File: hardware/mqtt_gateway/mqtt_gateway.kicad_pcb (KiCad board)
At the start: 2 copper layers, 75 x 51 mm, 54 parts, among them J1 awesome:RJ45-CAN, J3 RJ45_Amphenol_RJMG1BD3B8K1ANR, J4 WAGO250-204, Q1 BC847, Q2 BC847, U1 wuerthDebug6, U2 LD1117S33TR_SOT223, U3 PESD2CAN, U4 MCP2562-E-SN, U6 ESP32-WROOM-32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

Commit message: feat: Switch to 4 layer stackup
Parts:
- removed FB2: Ferrite_Bead_Small, Capacitor_SMD:C_0805_2012Metric_Pad1.18x1.45mm_HandSolder
- removed L1: 1m, Inductor_SMD:L_1210_3225Metric_Pad1.42x2.65mm_HandSolder
- added C7: 100n, Capacitor_SMD:C_0402_1005Metric_Pad0.74x0.62mm_HandSolder, F.Cu at (115.3, 109.5)
- added C8: 100n, Capacitor_SMD:C_0402_1005Metric_Pad0.74x0.62mm_HandSolder, F.Cu at (112.3, 103.8)
- added J2: Button-Sensors-MicroMatch2X03, awesome:02x03MicroMatch, F.Cu at (103.1, 89.7)
- added J5: Button-Sensors-MicroMatch2X03, awesome:02x03MicroMatch, F.Cu at (167.4, 86.5)
- added R1: 100R, Resistor_SMD:R_0603_1608Metric_Pad0.98x0.95mm_HandSolder, F.Cu at (111.0, 84.6)
- added R24: 100R, Resistor_SMD:R_0603_1608Metric_Pad0.98x0.95mm_HandSolder, F.Cu at (175.4, 81.5)
- added R25: 10K, Resistor_SMD:R_0603_1608Metric_Pad0.98x0.95mm_HandSolder, F.Cu at (126.9, 113.6)
- added R28: 10K, Resistor_SMD:R_0603_1608Metric_Pad0.98x0.95mm_HandSolder, F.Cu at (117.6, 110.6)
- added R29: 100R, Resistor_SMD:R_0603_1608Metric_Pad0.98x0.95mm_HandSolder, F.Cu at (176.2, 93.6)
- added R30: 100R, Resistor_SMD:R_0603_1608Metric_Pad0.98x0.95mm_HandSolder, F.Cu at (172.7, 81.5)
- added R31: 100R, Resistor_SMD:R_0603_1608Metric_Pad0.98x0.95mm_HandSolder, F.Cu at (173.9, 93.3)
- added R4: 100R, Resistor_SMD:R_0603_1608Metric_Pad0.98x0.95mm_HandSolder, F.Cu at (108.5, 84.6)
- added R5: 100R, Resistor_SMD:R_0603_1608Metric_Pad0.98x0.95mm_HandSolder, F.Cu at (107.1, 96.4)
- C12: value 1n -> 10u
- C14, C15, C17: footprint Capacitor_SMD:C_0603_1608Metric_Pad1.08x0.95mm_HandSolder -> Capacitor_SMD:C_0402_1005Metric_Pad0.74x0.62mm_HandSolder
- C16: value 1n -> 1u; footprint Capacitor_SMD:C_0603_1608Metric_Pad1.08x0.95mm_HandSolder -> Capacitor_SMD:C_0402_1005Metric_Pad0.74x0.62mm_HandSolder
- R16, R2: footprint Resistor_SMD:R_0603_1608Metric_Pad0.98x0.95mm_HandSolder -> Resistor_SMD:R_0402_1005Metric_Pad0.72x0.64mm_HandSolder
- R18: footprint Resistor_SMD:R_0603_1608Metric_Pad0.98x0.95mm_HandSolder -> Resistor_SMD:R_0402_1005Metric_Pad0.72x0.64mm_HandSolder; moved to F.Cu
- R3: value 33R -> 100R
- moved R9 39.0 mm to (134.8, 74.5), turned to -90 degrees
- moved R16 38.3 mm to (113.3, 109.5), turned to 90 degrees
- moved R6 24.6 mm to (126.1, 102.9), turned to 180 degrees
- moved R3 23.3 mm to (109.6, 96.4), turned to -90 degrees
- moved R8 21.7 mm to (113.4, 81.3), turned to 90 degrees
- moved R19 16.9 mm to (126.1, 101.4), turned to 180 degrees
- moved FB1 12.8 mm to (117.6, 98.8), turned to 90 degrees
- moved R2 11.4 mm to (114.3, 109.5), turned to 90 degrees
- moved C17 6.33 mm to (117.6, 102.7), turned to 0 degrees
- moved C16 5.98 mm to (117.6, 101.7)
- moved R18 5.78 mm to (116.3, 110.0), turned to -90 degrees
- moved C9 4.92 mm to (158.0, 89.4), turned to 180 degrees
- moved C18 4.83 mm to (122.6, 94.2), turned to 180 degrees
- moved C15 3.35 mm to (111.6, 108.1)
- moved C1 3.25 mm to (166.3, 90.0)
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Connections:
- net Net-(R16-Pad1) renamed /RXD1
- net Net-(R19-Pad2) renamed /ETHCLK_50M
- net Net-(U6-Pad33) renamed /TXEN
- C16 pad 1: Net-(C16-Pad1) -> VDDA
- C17 pad 1: Net-(C16-Pad1) -> VDDA
- FB1 pad 1: +3.3V -> VDDA
- FB1 pad 2: Net-(FB1-Pad2) -> +3.3V
- R18 pad 1: Net-(R18-Pad1) -> /RXER
- R18 pad 2: VDDA -> +3.3V
- R2 pad 1: Net-(R2-Pad1) -> /RXD0
- R3 pad 1: Net-(R3-Pad1) -> Net-(J2-Pad4)
- R3 pad 2: Net-(R3-Pad2) -> /B2-0/SCL
- R6 pad 1: Net-(R6-Pad1) -> /NRST
- U6 pad 10: Net-(U6-Pad10) -> /RXD0
- U6 pad 12: Net-(R18-Pad1) -> /CRS
- U6 pad 23: unconnected-(U6-Pad23) -> /B3-0
- U6 pad 24: unconnected-(U6-Pad24) -> /B2-0/SCL
- U6 pad 26: /SCK -> /B1-0/SDA
- U6 pad 27: unconnected-(U6-Pad27) -> /B4-0
- U6 pad 29: /SS -> /NRST
- U6 pad 30: Net-(U6-Pad30) -> /MDIO
- U6 pad 31: Net-(U6-Pad31) -> /TXD0
- U6 pad 36: Net-(R2-Pad1) -> /TXD1
- U6 pad 37: Net-(R3-Pad1) -> /MDC
- U6 pad 6: unconnected-(U6-Pad6) -> /B4-1
- U6 pad 7: unconnected-(U6-Pad7) -> /B3-1
- U6 pad 8: Net-(U6-Pad8) -> /B2-1/SCL
- U6 pad 9: Net-(R6-Pad1) -> /B1-1/SDA
- U7 pad 10: Net-(U6-Pad10) -> /RXER
- U7 pad 11: Net-(R16-Pad2) -> /CRS
- U7 pad 12: Net-(R18-Pad1) -> /MDIO
- U7 pad 13: Net-(U6-Pad8) -> /MDC
- U7 pad 15: Net-(R6-Pad1) -> /NRST
- U7 pad 17: Net-(U6-Pad30) -> /TXD0
- U7 pad 18: Net-(U6-Pad31) -> /TXD1
- U7 pad 7: Net-(R3-Pad2) -> Net-(R16-Pad2)
- U7 pad 9: Net-(FB1-Pad2) -> VDDA
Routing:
- net /B2-1/SCL: track 0.00 -> 52.9 mm, vias 0 -> 2
- net GND: track 51.5 -> 99.8 mm, vias 6 -> 22
- net /B3-1: track 0.00 -> 46.7 mm, vias 0 -> 2
- net /B1-1/SDA: track 0.00 -> 44.9 mm, vias 0 -> 2
- net /B3-0: track 0.00 -> 42.4 mm, vias 0 -> 2
- net Net-(R16-Pad2): track 43.9 -> 1.72 mm, vias 2 -> 0
- net /B1-0/SDA: track 0.00 -> 41.7 mm, vias 0 -> 2
- net +3.3V: track 170.2 -> 210.8 mm, vias 5 -> 9
- net Net-(R6-Pad1): track 39.6 -> 0.00 mm, vias 2 -> 0
- net /RXD0: track 0.00 -> 38.1 mm, vias 0 -> 2
- net /RXD1: track 3.52 -> 41.3 mm, vias 0 -> 2
- net Net-(U6-Pad10): track 37.2 -> 0.00 mm, vias 2 -> 0
- net Net-(R18-Pad1): track 36.4 -> 0.00 mm, vias 2 -> 0
- net /CRS: track 0.00 -> 35.5 mm, vias 0 -> 2
- net Net-(U6-Pad8): track 34.3 -> 0.00 mm, vias 2 -> 0
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- added copper zone on In1.Cu, net GND
- added copper zone on In2.Cu, net GND
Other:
- copper layers 2 -> 4

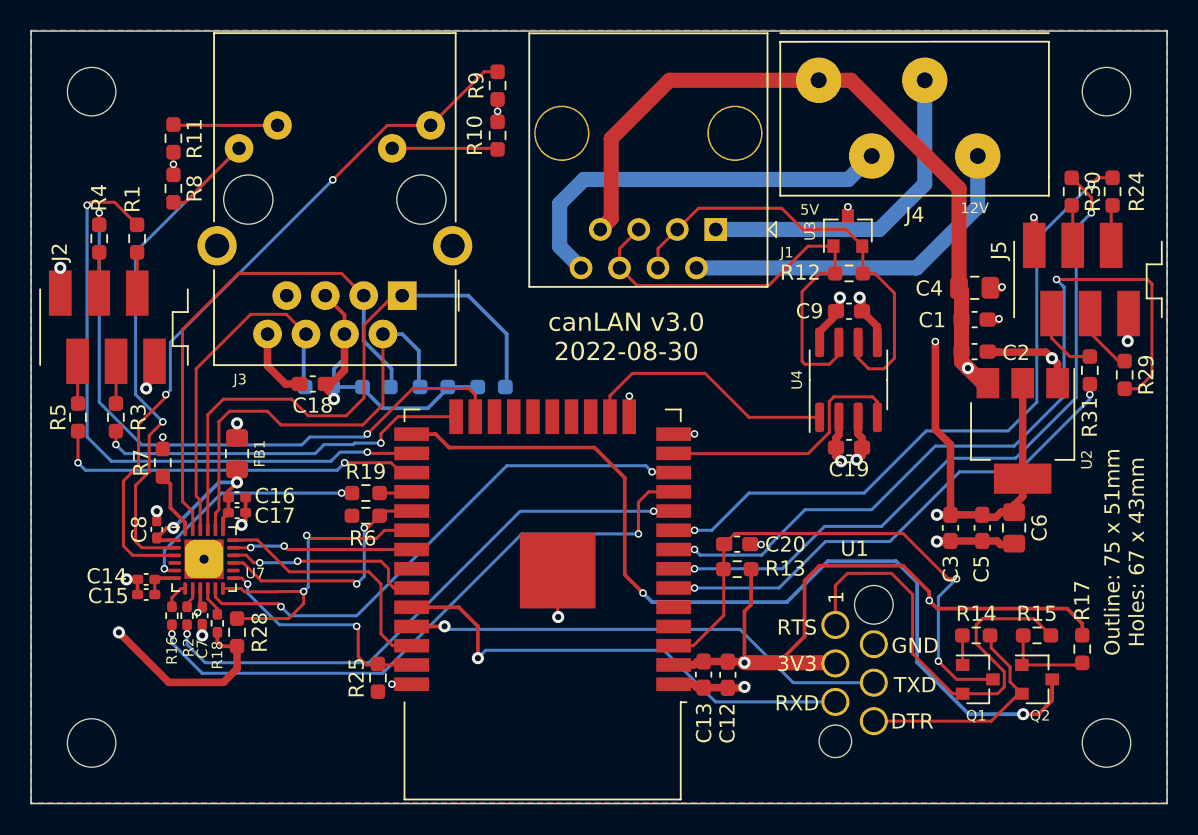
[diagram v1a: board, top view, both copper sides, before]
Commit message: style: Move traces
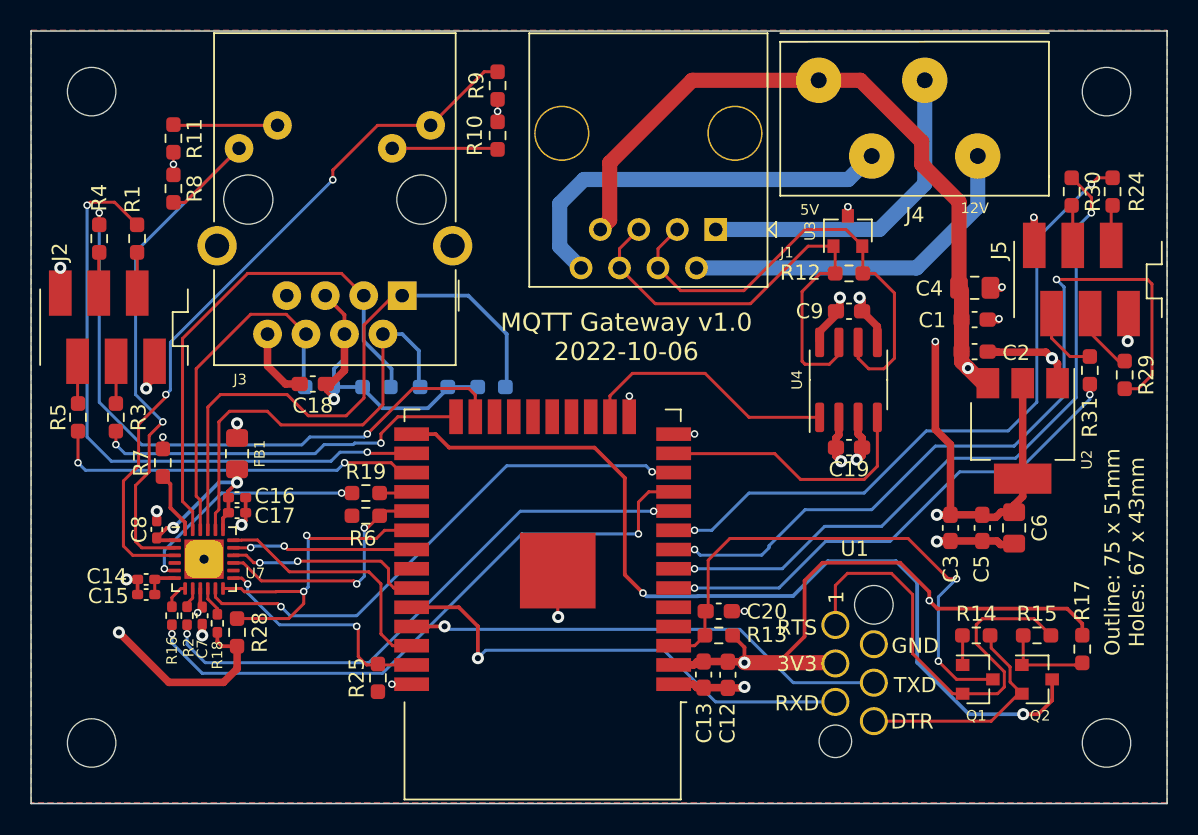
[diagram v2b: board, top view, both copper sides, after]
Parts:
- moved C20 4.59 mm to (149.4, 109.2)
- moved R13 4.54 mm to (149.4, 110.8)
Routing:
- net +3.3V: track 210.8 -> 206.7 mm
- net Net-(J1-Pad3): track 29.7 -> 32.1 mm
- net Net-(J1-Pad5): track 31.5 -> 32.5 mm
- net Net-(J3-PadR1): track 38.9 -> 39.4 mm
- net +5V: track 61.9 -> 61.3 mm
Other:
- board text added: "MQTT Gateway v1.0 2022-10-06"
- board text removed: "canLAN v3.0 2022-08-30"

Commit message: feat: change PCB debug to EN/BOOT0
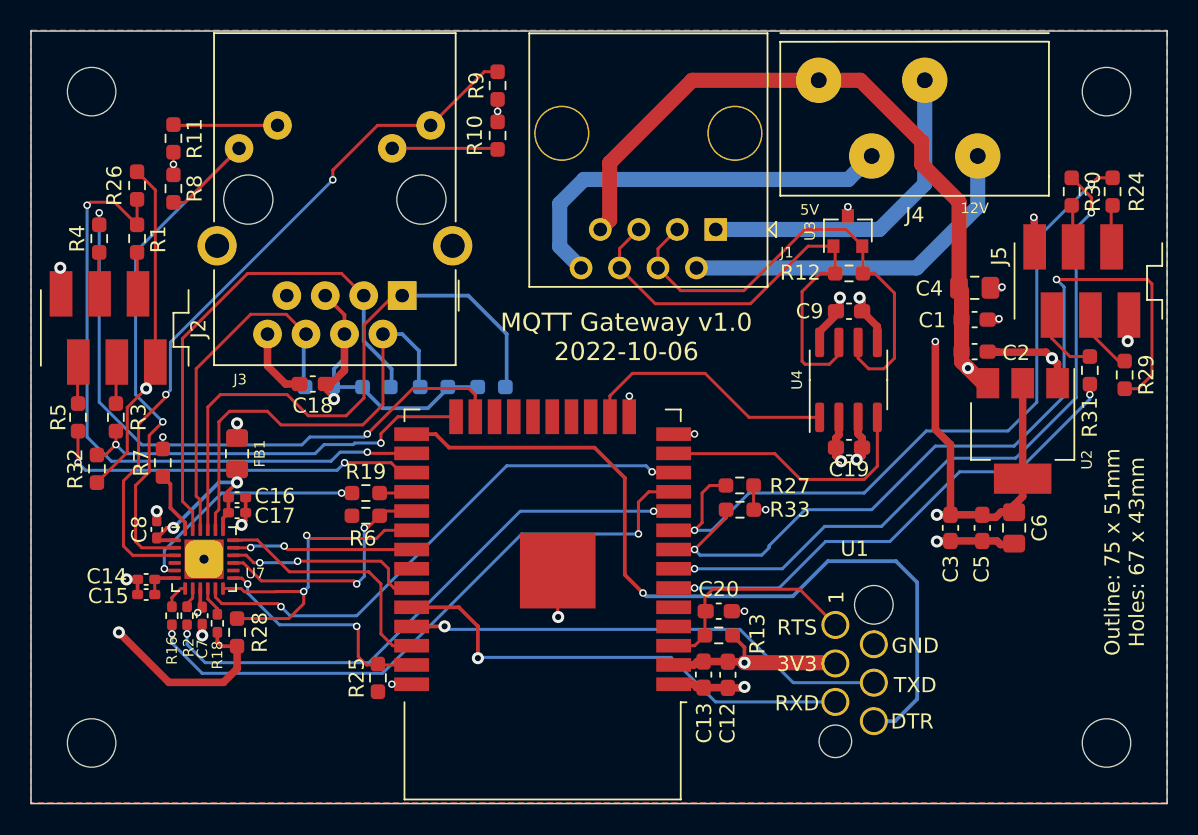
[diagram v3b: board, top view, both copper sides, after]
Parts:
- removed Q1, Q2: BC847, Package_TO_SOT_SMD:SOT-23
- removed R14, R15, R17: 10K, Resistor_SMD:R_0603_1608Metric_Pad0.98x0.95mm_HandSolder
- added R26: 2K2, Resistor_SMD:R_0603_1608Metric_Pad0.98x0.95mm_HandSolder, F.Cu at (111.0, 81.1)
- added R27: 2K2, Resistor_SMD:R_0603_1608Metric_Pad0.98x0.95mm_HandSolder, F.Cu at (150.8, 100.9)
- added R32: 2K2, Resistor_SMD:R_0603_1608Metric_Pad0.98x0.95mm_HandSolder, F.Cu at (108.3, 99.8)
- added R33: 2K2, Resistor_SMD:R_0603_1608Metric_Pad0.98x0.95mm_HandSolder, F.Cu at (150.8, 102.5)
- moved J2 6.08 mm to (109.1, 90.5), turned to -90 degrees
- moved J5 6.06 mm to (173.4, 87.4), turned to -90 degrees
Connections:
- J2 pad 1: GND -> +3.3V
- J2 pad 6: +3.3V -> GND
- J5 pad 1: GND -> +3.3V
- J5 pad 6: +3.3V -> GND
- R1 pad 1: Net-(J2-Pad5) -> Net-(J2-Pad2)
- R24 pad 1: Net-(J5-Pad5) -> Net-(J5-Pad2)
- R29 pad 1: Net-(J5-Pad4) -> Net-(J5-Pad3)
- R3 pad 1: Net-(J2-Pad4) -> Net-(J2-Pad3)
- R30 pad 1: Net-(J5-Pad3) -> Net-(J5-Pad4)
- R31 pad 1: Net-(J5-Pad2) -> Net-(J5-Pad5)
- R4 pad 1: Net-(J2-Pad3) -> Net-(J2-Pad4)
- R5 pad 1: Net-(J2-Pad2) -> Net-(J2-Pad5)
- U1 pad 1: /RTS -> /EN
- U1 pad 6: /DTR -> /BOOT0
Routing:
- net /RTS: track 30.3 -> 0.00 mm
- net /EN: track 36.6 -> 15.8 mm, vias 2 -> 0
- net /DTR: track 15.0 -> 0.00 mm
- net /BOOT0: track 60.3 -> 54.1 mm, vias 2 -> 1
- net Net-(Q2-Pad1): track 5.54 -> 0.00 mm
- net +3.3V: track 206.7 -> 201.2 mm
- net /B1-1/SDA: track 44.9 -> 49.4 mm
- net Net-(J5-Pad5): track 1.69 -> 5.63 mm
- net Net-(J5-Pad2): track 5.63 -> 1.69 mm
- net Net-(J5-Pad4): track 5.31 -> 1.69 mm
- net Net-(J5-Pad3): track 1.69 -> 5.31 mm
- net /B2-1/SCL: track 52.9 -> 56.4 mm
- net Net-(Q1-Pad1): track 1.75 -> 0.00 mm
- net /B1-0/SDA: track 41.7 -> 43.3 mm
- net /B2-0/SCL: track 25.0 -> 26.5 mm

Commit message: feat: Add fab export options for all pcbs
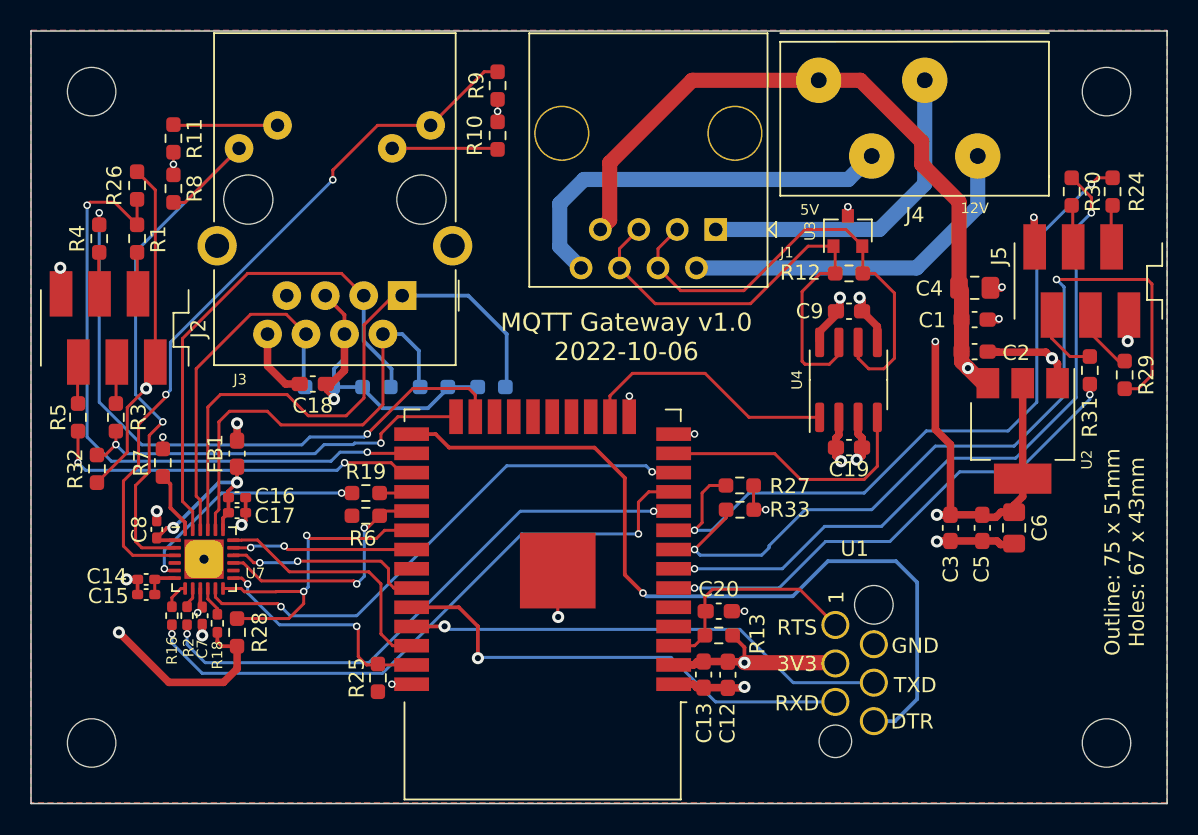
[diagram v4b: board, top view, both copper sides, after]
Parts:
- FB1: footprint Capacitor_SMD:C_0805_2012Metric_Pad1.18x1.45mm_HandSolder -> Capacitor_SMD:C_0603_1608Metric_Pad1.08x0.95mm_HandSolder
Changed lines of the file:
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@@
       (layerselection 0x00010fc_ffffffff)
       (disableapertmacros false)
-      (usegerberextensions true)
-      (usegerberattributes false)
+      (usegerberextensions false)
+      (usegerberattributes true)
       (usegerberadvancedattributes true)
-      (creategerberjobfile false)
+      (creategerberjobfile true)
       (svguseinch false)
       (svgprecision 6)
@@
       (plotinvisibletext false)
       (sketchpadsonfab false)
-      (subtractmaskfromsilk false)
+      (subtractmaskfromsilk true)
       (outputformat 1)
       (mirror false)
       (drillshape 0)
       (scaleselection 1)
-      (outputdirectory "fab")
+      (outputdirectory "mqtt_gateway-fab")
     )
   )
@@
     )
   )
-  (footprint "Capacitor_SMD:C_0805_2012Metric_Pad1.18x1.45mm_HandSolder" (layer "F.Cu")
+  (footprint "Capacitor_SMD:C_0603_1608Metric_Pad1.08x0.95mm_HandSolder" (layer "F.Cu")
     (at 117.6 98.8 90)
-    (descr "Capacitor SMD 0805 (2012 Metric), square (rectangular) end terminal, IPC_7351 nominal with elongated pad for handsoldering. (Body size source: IPC-SM-782 page 76, https://www.pcb-3d.com/wordpress/wp-content/uploads/ipc-sm-782a_amendment_1_and_2.pdf, https://docs.google.com/spreadsheets/d/1BsfQQcO9C6DZCsRaXUlFlo91Tg2WpOkGARC1WS5S8t0/edit?usp=sharing), generated with kicad-footprint-generator")
+    (descr "Capacitor SMD 0603 (1608 Metric), square (rectangular) end terminal, IPC_7351 nominal with elongated pad for handsoldering. (Body size source: IPC-SM-782 page 76, https://www.pcb-3d.com/wordpress/wp-content/uploads/ipc-sm-782a_amendment_1_and_2.pdf), generated with kicad-footprint-generator")
     (tags "capacitor handsolder")
     (property "Sheetfile" "mqtt_gateway.kicad_sch")
     (property "Sheetname" "")
     (attr smd)
-    (fp_text reference "FB1" (at 0 1.5 90) (layer "F.SilkS")
-      (effects (font (size 0.7 0.7) (thickness 0.1)))
-    )
-    (fp_text value "Ferrite_Bead_Small" (at 0 1.68 90) (layer "F.Fab")
+    (fp_text reference "FB1" (at 0 -1.43 90) (layer "F.SilkS")
+      (effects (font (size 1 1) (thickness 0.15)))
+    )
+    (fp_text value "Ferrite_Bead_Small" (at 0 1.43 90) (layer "F.Fab")
       (effects (font (size 1 1) (thickness 0.15)))
     )
     (fp_text user "${REFERENCE}" (at 0 0 90) (layer "F.Fab")
-      (effects (font (size 0.5 0.5) (thickness 0.08)))
-    )
-    (fp_line (start -0.261252 0.735) (end 0.261252 0.735) (layer "F.SilkS") (width 0.12))
-    (fp_line (start -0.261252 -0.735) (end 0.261252 -0.735) (layer "F.SilkS") (width 0.12))
-    (fp_line (start 1.88 -0.98) (end 1.88 0.98) (layer "F.CrtYd") (width 0.05))
-    (fp_line (start -1.88 0.98) (end -1.88 -0.98) (layer "F.CrtYd") (width 0.05))
-    (fp_line (start 1.88 0.98) (end -1.88 0.98) (layer "F.CrtYd") (width 0.05))
-    (fp_line (start -1.88 -0.98) (end 1.88 -0.98) (layer "F.CrtYd") (width 0.05))
-    (fp_line (start 1 -0.625) (end 1 0.625) (layer "F.Fab") (width 0.1))
-    (fp_line (start -1 0.625) (end -1 -0.625) (layer "F.Fab") (width 0.1))
-    (fp_line (start 1 0.625) (end -1 0.625) (layer "F.Fab") (width 0.1))
-    (fp_line (start -1 -0.625) (end 1 -0.625) (layer "F.Fab") (width 0.1))
-    (pad "1" smd roundrect locked (at -1.0375 0 90) (size 1.175 1.45) (layers "F.Cu" "F.Paste" "F.Mask") (roundrect_rratio 0.2127659574)
+      (effects (font (size 0.4 0.4) (thickness 0.06)))
+    )
+    (fp_line (start -0.146267 -0.51) (end 0.146267 -0.51) (layer "F.SilkS") (width 0.12))
+    (fp_line (start -0.146267 0.51) (end 0.146267 0.51) (layer "F.SilkS") (width 0.12))
+    (fp_line (start -1.65 -0.73) (end 1.65 -0.73) (layer "F.CrtYd") (width 0.05))
+    (fp_line (start 1.65 0.73) (end -1.65 0.73) (layer "F.CrtYd") (width 0.05))
+    (fp_line (start 1.65 -0.73) (end 1.65 0.73) (layer "F.CrtYd") (width 0.05))
+    (fp_line (start -1.65 0.73) (end -1.65 -0.73) (layer "F.CrtYd") (width 0.05))
+    (fp_line (start 0.8 -0.4) (end 0.8 0.4) (layer "F.Fab") (width 0.1))
+    (fp_line (start 0.8 0.4) (end -0.8 0.4) (layer "F.Fab") (width 0.1))
+    (fp_line (start -0.8 0.4) (end -0.8 -0.4) (layer "F.Fab") (width 0.1))
+    (fp_line (start -0.8 -0.4) (end 0.8 -0.4) (layer "F.Fab") (width 0.1))
+    (pad "1" smd roundrect (at -0.8625 0 90) (size 1.075 0.95) (layers "F.Cu" "F.Paste" "F.Mask") (roundrect_rratio 0.25)
       (net 4 "VDDA") (pintype "passive"))
-    (pad "2" smd roundrect locked (at 1.0375 0 90) (size 1.175 1.45) (layers "F.Cu" "F.Paste" "F.Mask") (roundrect_rratio 0.2127659574)
+    (pad "2" smd roundrect (at 0.8625 0 90) (size 1.075 0.95) (layers "F.Cu" "F.Paste" "F.Mask") (roundrect_rratio 0.25)
       (net 3 "+3.3V") (pintype "passive"))
-    (model "${KISYS3DMOD}/Capacitor_SMD.3dshapes/C_0805_2012Metric.wrl"
+    (model "${KICAD6_3DMODEL_DIR}/Capacitor_SMD.3dshapes/C_0603_1608Metric.wrl"
       (offset (xyz 0 0 0))
       (scale (xyz 1 1 1))
@@
     (fp_line (start -1 -0.625) (end 1 -0.625) (layer "F.Fab") (width 0.1))
     (fp_line (start -1 0.625) (end -1 -0.625) (layer "F.Fab") (width 0.1))
-    (pad "1" smd roundrect (at -1.0375 0) (size 1.175 1.45) (layers "F.Cu" "F.Paste" "F.Mask") (roundrect_rratio 0.212766)
+    (pad "1" smd roundrect (at -1.0375 0) (size 1.175 1.45) (layers "F.Cu" "F.Paste" "F.Mask") (roundrect_rratio 0.2127659574)
       (net 2 "+5V") (pintype "passive"))
-    (pad "2" smd roundrect (at 1.0375 0) (size 1.175 1.45) (layers "F.Cu" "F.Paste" "F.Mask") (roundrect_rratio 0.212766)
+    (pad "2" smd roundrect (at 1.0375 0) (size 1.175 1.45) (layers "F.Cu" "F.Paste" "F.Mask") (roundrect_rratio 0.2127659574)
       (net 1 "GND") (pintype "passive"))
     (model "${KICAD6_3DMODEL_DIR}/Capacitor_SMD.3dshapes/C_0805_2012Metric.wrl"
@@
     (fp_line (start 1 -0.625) (end 1 0.625) (layer "F.Fab") (width 0.1))
     (fp_line (start -1 -0.625) (end 1 -0.625) (layer "F.Fab") (width 0.1))
-    (pad "1" smd roundrect (at -1.0375 0 270) (size 1.175 1.45) (layers "F.Cu" "F.Paste" "F.Mask") (roundrect_rratio 0.212766)
+    (pad "1" smd roundrect (at -1.0375 0 270) (size 1.175 1.45) (layers "F.Cu" "F.Paste" "F.Mask") (roundrect_rratio 0.2127659574)
       (net 3 "+3.3V") (pintype "passive"))
-    (pad "2" smd roundrect (at 1.0375 0 270) (size 1.175 1.45) (layers "F.Cu" "F.Paste" "F.Mask") (roundrect_rratio 0.212766)
+    (pad "2" smd roundrect (at 1.0375 0 270) (size 1.175 1.45) (layers "F.Cu" "F.Paste" "F.Mask") (roundrect_rratio 0.2127659574)
       (net 1 "GND") (pintype "passive"))
     (model "${KICAD6_3DMODEL_DIR}/Capacitor_SMD.3dshapes/C_0805_2012Metric.wrl"
